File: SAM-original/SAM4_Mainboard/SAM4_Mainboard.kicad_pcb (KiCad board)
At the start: 4 copper layers, 111.7 x 142.2 mm, 69 parts, among them J1 Conn_01x04_Female, J11 Conn_01x02_Female, J12 10103594-0001LF, J13 Conn_01x04_Female, J14 Conn_01x04_Female, J15 Conn_01x04_Female, J16 Conn_01x04_Female, J17 Conn_01x04_Female, J2 Conn_01x04_Female, J3 Conn_01x04_Female, J4 Conn_01x04_Female, J5 Conn_01x04_Female, J6 XT60PW-M, J7 XT60PW-M, J8 XT30PW-F, J9 Conn_02x16_Odd_Even, M1 MR30PW-FB, M2 MR30PW-FB, M3 MR30PW-FB, M4 MR30PW-FB, SW1 SW_SPST, U1 SN74LV1T34DBV, U2 T-motor_F55A_PROII, U3 BM10B-SRSS-TB, U4 i3A4W005A150V, U5 Cube_PSM, U6 i3A4W005A150V, U7 LM3480-3.3, U8 ACS71240LLCBTR-030B3

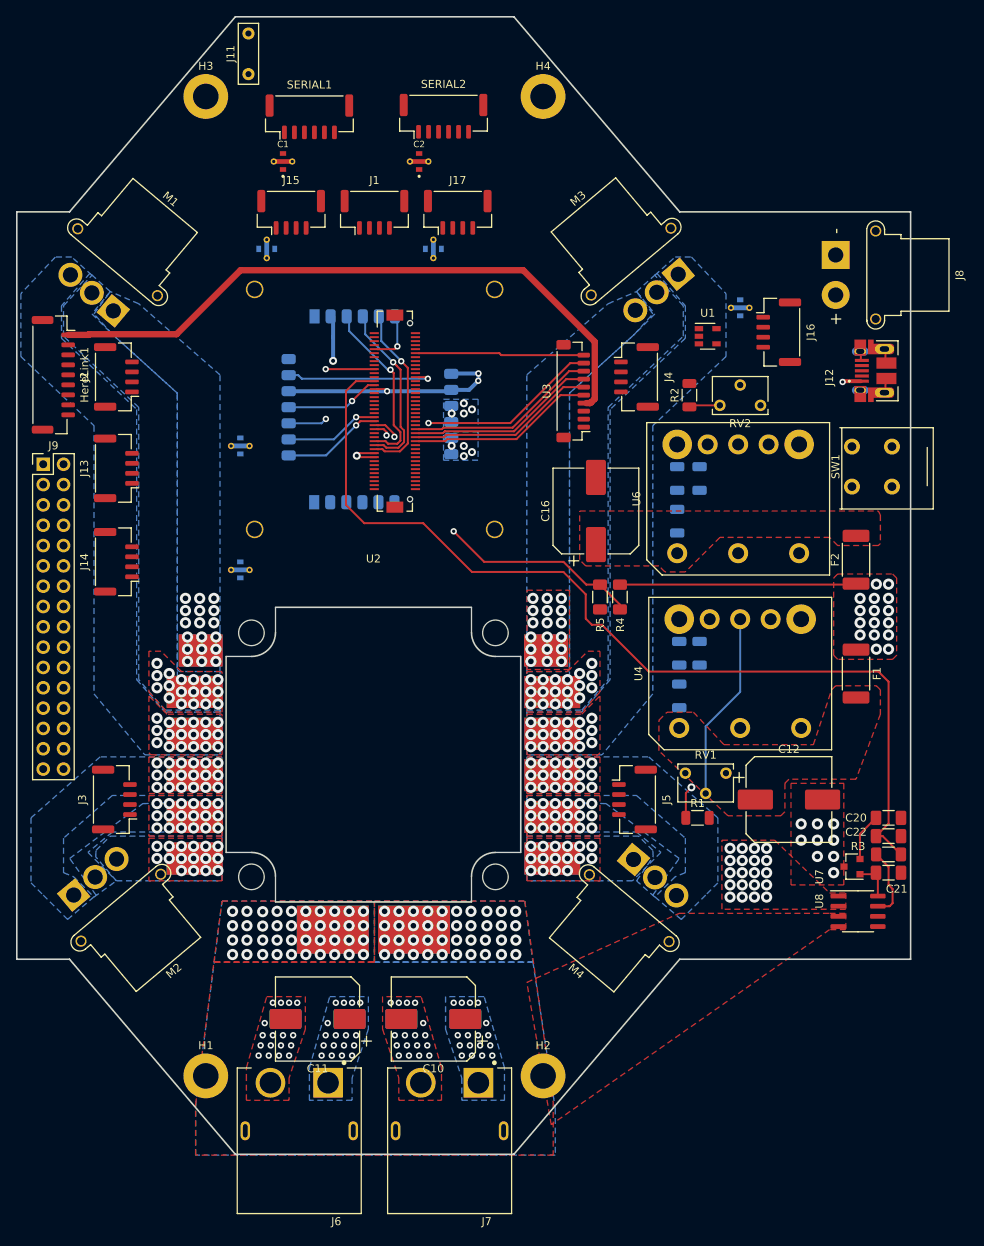
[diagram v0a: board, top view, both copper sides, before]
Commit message: add production files for EasyLAM PDB, STEP for EasySAM
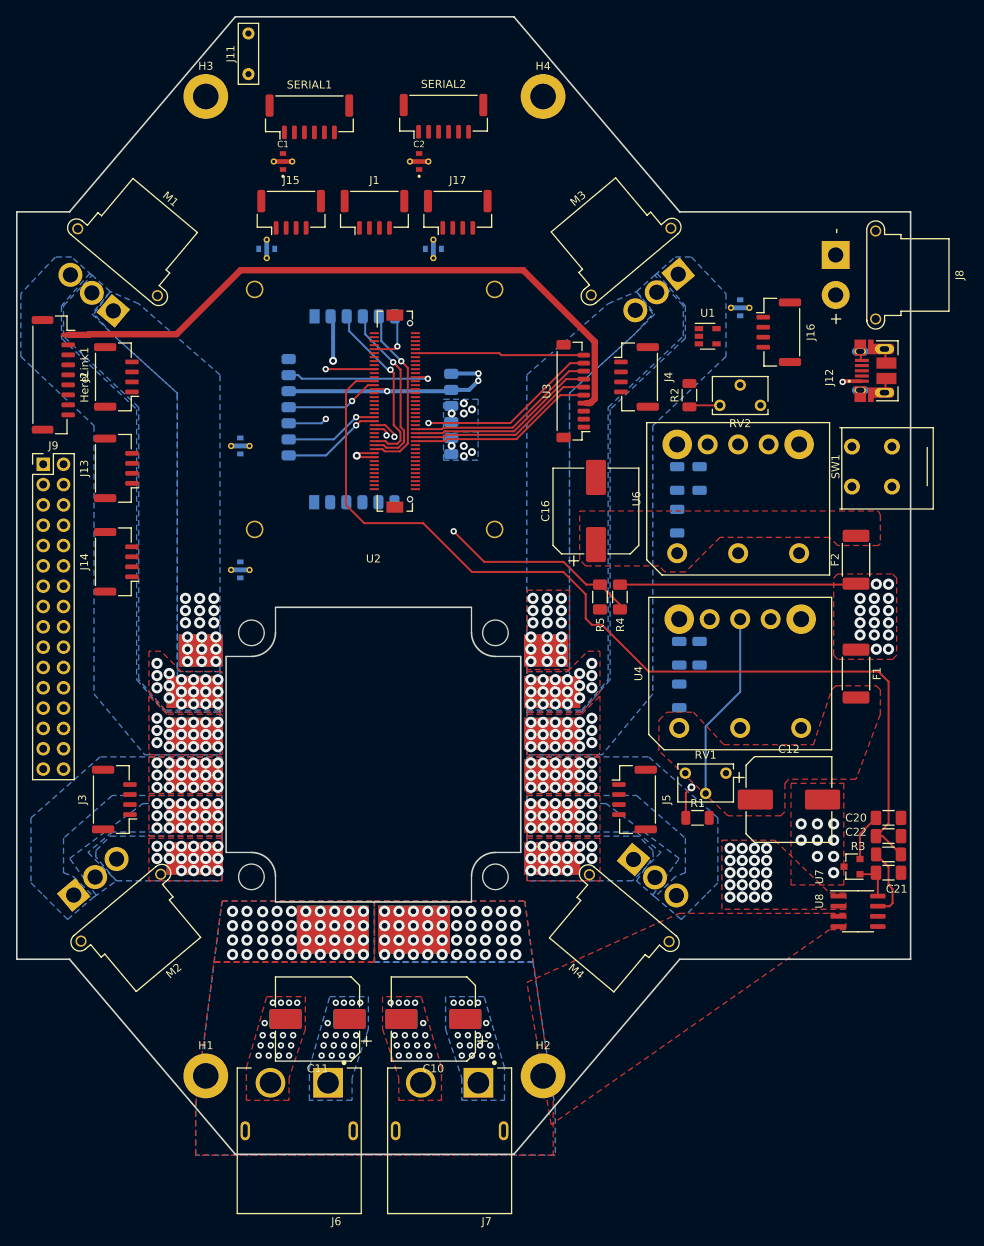
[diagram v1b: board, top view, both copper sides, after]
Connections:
- net FMU-~RESET renamed FMU-~{RESET}
- net ~EXTERN_CS renamed ~{EXTERN_CS}
- net ~FMU-LED_AMBER renamed ~{FMU-LED_AMBER}
- net ~IO-LED_SAFETY_PROT renamed ~{IO-LED_SAFETY_PROT}
- net ~VBUS_VALID renamed ~{VBUS_VALID}
- net ~VDD_5V_PERIPH_EN renamed ~{VDD_5V_PERIPH_EN}
- net ~VDD_5V_PERIPH_OC renamed ~{VDD_5V_PERIPH_OC}
- net ~VDD_BACKUP_VALID renamed ~{VDD_BACKUP_VALID}
- net ~VDD_BRICK_VALID renamed ~{VDD_BRICK_VALID}
- net ~VDD_HIPOWER_OC renamed ~{VDD_HIPOWER_OC}
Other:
- net class Default removed
